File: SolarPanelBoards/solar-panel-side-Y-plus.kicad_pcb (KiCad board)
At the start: 2 copper layers, 82 x 99 mm, 24 parts, among them J1 Conn_01x06, U1 OPT3001DNPT

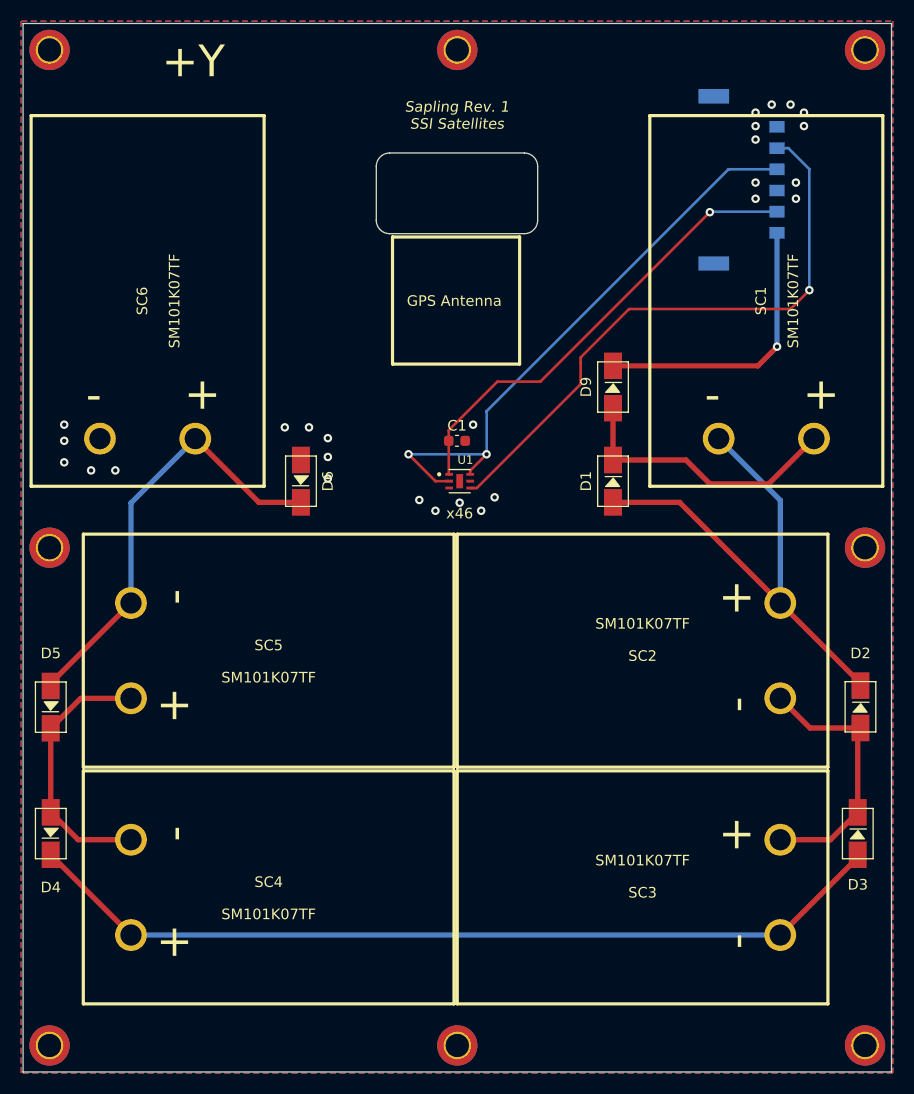
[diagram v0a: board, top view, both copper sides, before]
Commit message: Battery board and side panels ready for CAD check and review, pycubed not finished yet
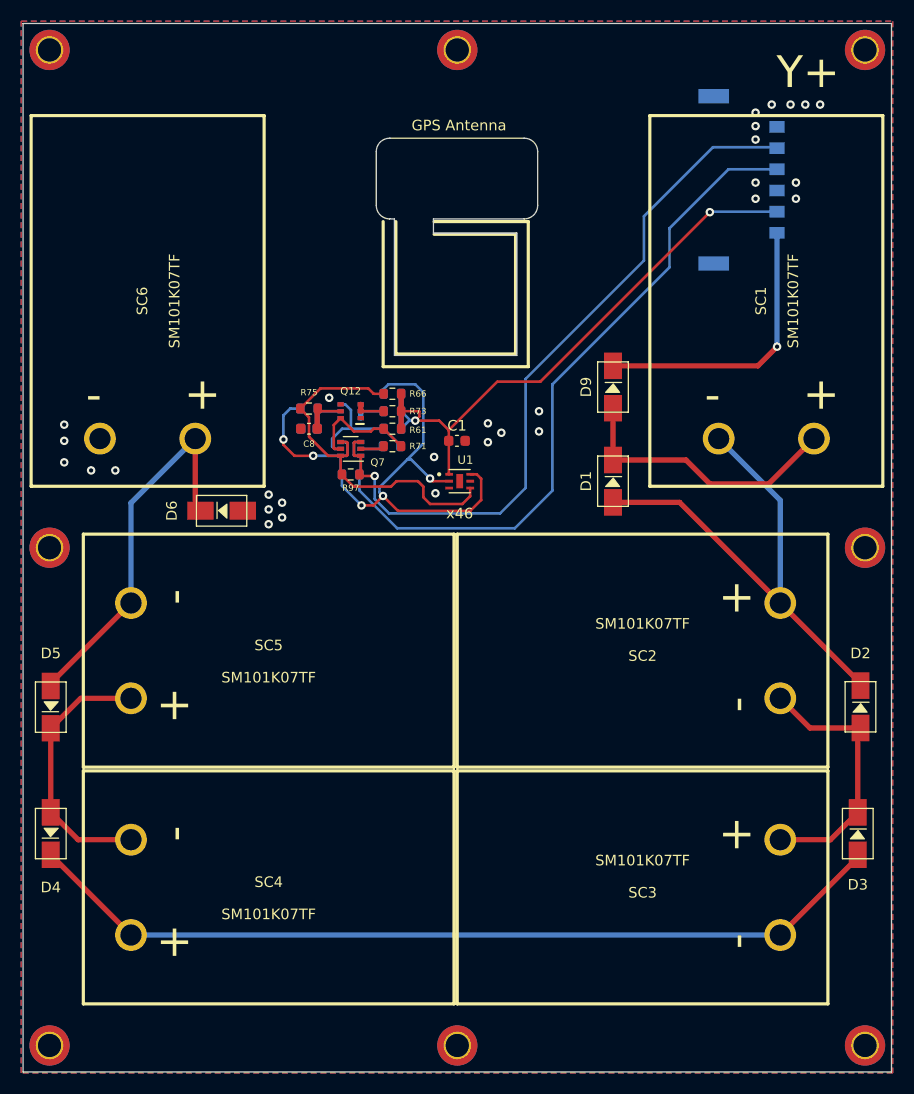
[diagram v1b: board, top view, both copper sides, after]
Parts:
- added C40: 10nF, Capacitor_SMD:C_0603_1608Metric, B.Cu at (134.6, 81.9)
- added C8: 10nF, Capacitor_SMD:C_0603_1608Metric, F.Cu at (134.6, 81.9)
- added Q12: BSS138DWQ-7, sapling:BSS138DWQ-7, F.Cu at (138.6, 80.3)
- added Q13: BSS138DWQ-7, sapling:BSS138DWQ-7, B.Cu at (138.6, 80.3)
- added Q7: MBT2222ADW1T1, Package_TO_SOT_SMD:SOT-363_SC-70-6, F.Cu at (138.6, 83.8)
- added Q8: MBT2222ADW1T1, Package_TO_SOT_SMD:SOT-363_SC-70-6, B.Cu at (138.6, 83.8)
- added R61: 10K, Resistor_SMD:R_0603_1608Metric, F.Cu at (142.5, 81.9)
- added R62: 10K, Resistor_SMD:R_0603_1608Metric, B.Cu at (142.5, 81.9)
- added R66: 10K, Resistor_SMD:R_0603_1608Metric, F.Cu at (142.5, 78.6)
- added R67: 10K, Resistor_SMD:R_0603_1608Metric, B.Cu at (142.5, 78.6)
- added R71: 680, Resistor_SMD:R_0603_1608Metric, F.Cu at (142.5, 83.6)
- added R72: 680, Resistor_SMD:R_0603_1608Metric, B.Cu at (142.4, 83.6)
- added R73: 100K, Resistor_SMD:R_0603_1608Metric, F.Cu at (142.5, 80.3)
- added R74: 100K, Resistor_SMD:R_0603_1608Metric, B.Cu at (142.5, 80.3)
- added R75: 200K, Resistor_SMD:R_0603_1608Metric, F.Cu at (134.6, 80.0)
- added R76: 200K, Resistor_SMD:R_0603_1608Metric, B.Cu at (134.6, 80.0)
- added R97: 0, Resistor_SMD:R_0603_1608Metric, F.Cu at (138.6, 86.2)
- added R98: 0, Resistor_SMD:R_0603_1608Metric, B.Cu at (138.6, 86.2)
- added REF**: AP.12F_Taoglas, sapling:AP.12F_Taoglas, F.Cu at (149.0, 61.1)
- moved D6 8.00 mm to (126.4, 89.7), turned to 0 degrees
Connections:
- U1 pad 2: SDA -> SDA_SUN
- U1 pad 4: SCL -> SCL_SUN
- U1 pad 6: SDA -> SDA_SUN
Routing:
- net SDA_SUN: track 0.00 -> 55.5 mm, vias 0 -> 5
- net SCL_SUN: track 0.00 -> 35.3 mm
- net +3V3: track 43.7 -> 60.0 mm, vias 1 -> 2
- net SDA: track 55.7 -> 68.8 mm, vias 2 -> 0
- net SCL: track 56.5 -> 69.4 mm
- net Net-(Q13-Pad6): track 0.00 -> 12.2 mm
- net Net-(Q12-Pad6): track 0.00 -> 10.8 mm
- net Net-(D5-Pad2): track 41.5 -> 36.0 mm
- net Net-(C8-Pad1): track 0.00 -> 4.19 mm
- net Net-(C40-Pad1): track 0.00 -> 4.19 mm
- net Net-(Q13-Pad2): track 0.00 -> 2.81 mm
- net Net-(Q12-Pad2): track 0.00 -> 2.81 mm
- net Net-(Q7-Pad2): track 0.00 -> 2.27 mm
- net Net-(Q8-Pad2): track 0.00 -> 2.20 mm
- net GND: vias 27 -> 29
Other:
- outline, holes or cut-outs redrawn
- board text added: "+3.3V"
- board text removed: "3.3"
- board text removed: "Sapling Rev. 1 SSI Satellites"

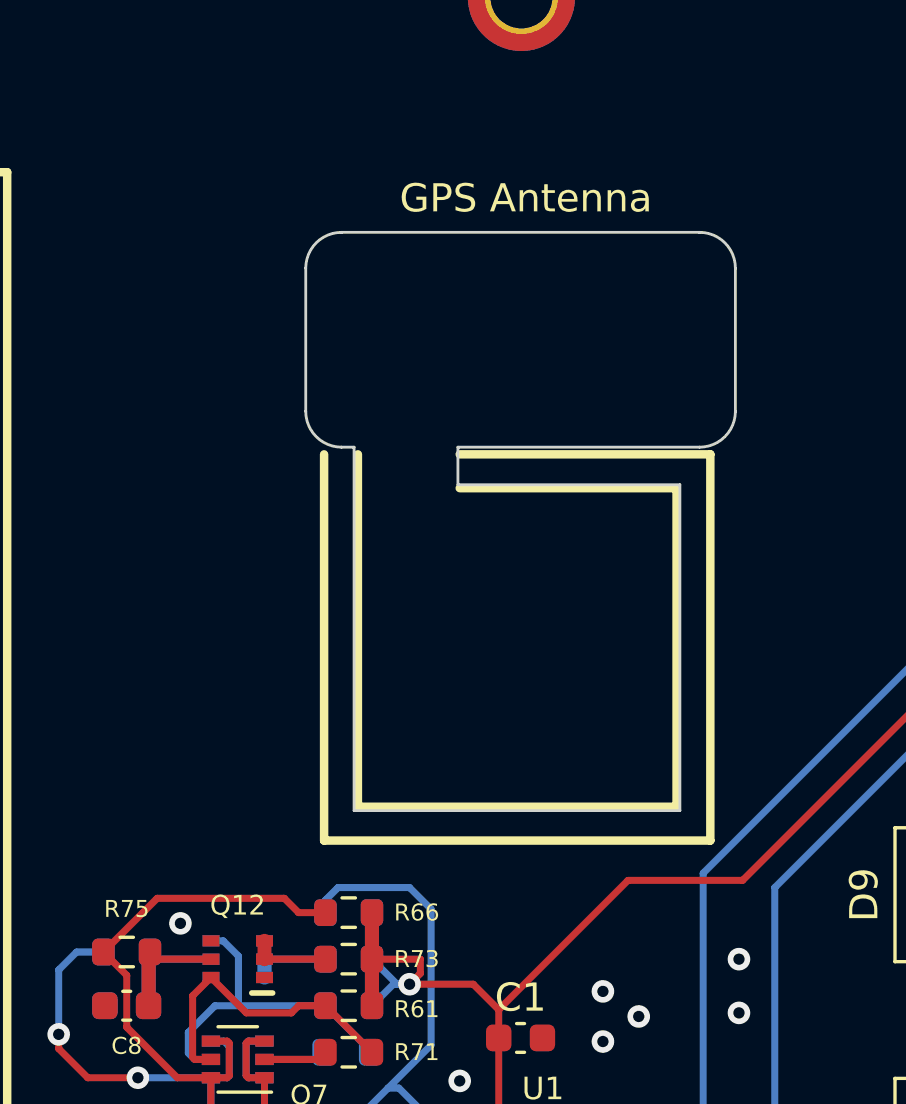
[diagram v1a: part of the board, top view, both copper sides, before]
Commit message: side panels ready except for RF trace width
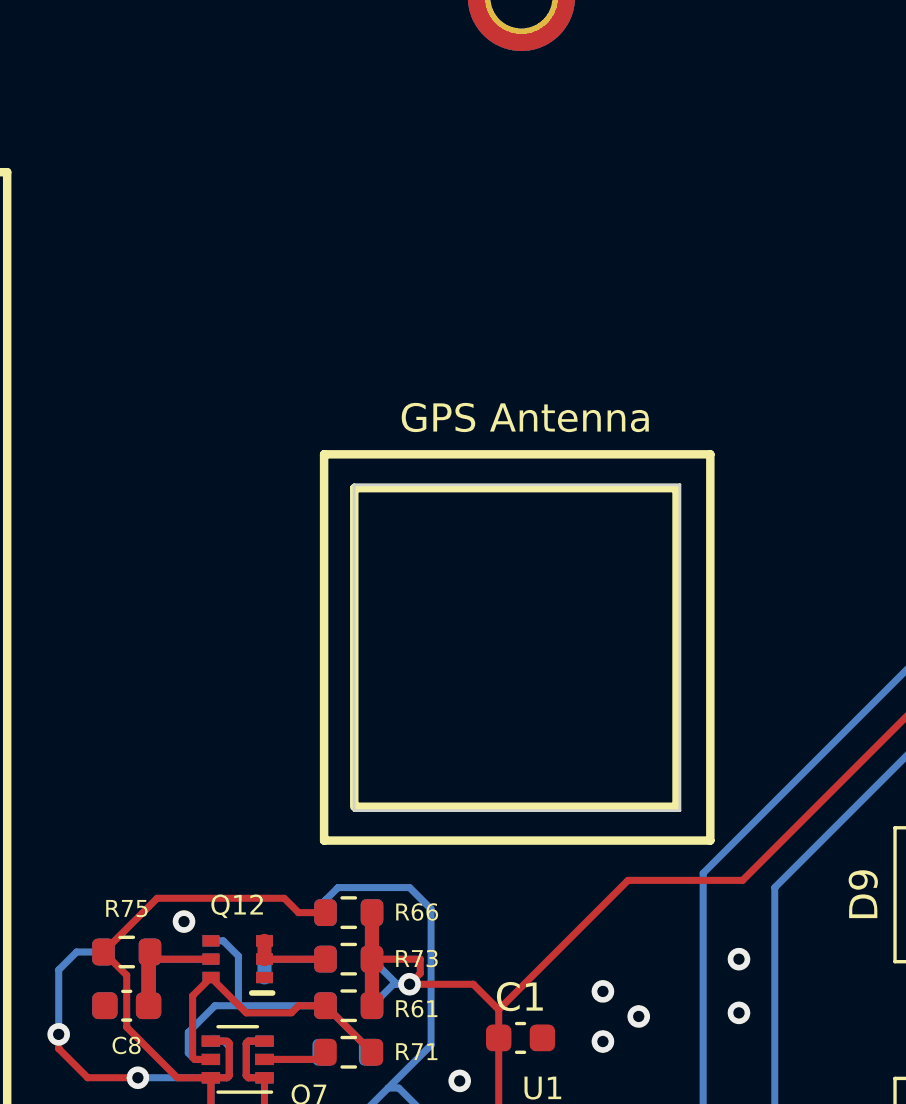
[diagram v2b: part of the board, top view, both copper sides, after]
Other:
- outline, holes or cut-outs redrawn
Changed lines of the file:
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@@
   (general
     (thickness 1.6)
-    (drawings 27)
+    (drawings 17)
     (tracks 244)
     (zones 0)
@@
       (effects (font (size 1 1) (thickness 0.15)))
     )
-    (fp_line (start -2.54 1.27) (end 6.35 1.27) (layer F.SilkS) (width 0.3))
+    (fp_line (start -6.28 13.77) (end -6.28 2.47) (layer F.SilkS) (width 0.3))
+    (fp_line (start -6.15 13.77) (end 5.15 13.77) (layer F.SilkS) (width 0.3))
+    (fp_line (start 5.15 13.77) (end 5.15 2.47) (layer F.SilkS) (width 0.3))
+    (fp_line (start -6.28 2.47) (end 5.15 2.47) (layer F.SilkS) (width 0.3))
+    (fp_line (start -7.35 14.97) (end -7.35 1.27) (layer F.SilkS) (width 0.3))
+    (fp_line (start -7.35 14.97) (end 6.35 14.97) (layer F.SilkS) (width 0.3))
     (fp_line (start 6.35 14.97) (end 6.35 1.27) (layer F.SilkS) (width 0.3))
-    (fp_line (start -7.35 14.97) (end 6.35 14.97) (layer F.SilkS) (width 0.3))
-    (fp_line (start -7.35 14.97) (end -7.35 1.27) (layer F.SilkS) (width 0.3))
-    (fp_line (start -2.54 2.47) (end 5.15 2.47) (layer F.SilkS) (width 0.3))
-    (fp_line (start -6.15 13.77) (end -6.15 1.27) (layer F.SilkS) (width 0.3))
-    (fp_line (start 5.15 13.77) (end 5.15 2.47) (layer F.SilkS) (width 0.3))
-    (fp_line (start -6.15 13.77) (end 5.15 13.77) (layer F.SilkS) (width 0.3))
+    (fp_line (start -7.35 1.27) (end 6.35 1.27) (layer F.SilkS) (width 0.3))
     (model C:/Users/grant/Downloads/AP.12F.07.0045A_Web_v2.step
-      (offset (xyz -4.75 20.3 70.7))
+      (offset (xyz -4.75 20.3 68.34999999999999))
       (scale (xyz 1 1 1))
       (rotate (xyz -180 0 -90))
@@
     )
   )
-  (gr_line (start 146.3675 62.103) (end 146.3675 63.4365) (layer Edge.Cuts) (width 0.1))
-  (gr_line (start 146.3675 62.103) (end 154.94 62.103) (layer Edge.Cuts) (width 0.1))
-  (gr_line (start 142.6845 74.9935) (end 142.6845 62.103) (layer Edge.Cuts) (width 0.1))
+  (gr_line (start 142.6845 74.9935) (end 142.6845 63.4365) (layer Edge.Cuts) (width 0.1))
   (gr_line (start 154.2415 74.9935) (end 142.6845 74.9935) (layer Edge.Cuts) (width 0.1))
   (gr_line (start 154.2415 63.4365) (end 154.2415 74.9935) (layer Edge.Cuts) (width 0.1))
-  (gr_line (start 146.3675 63.4365) (end 154.2415 63.4365) (layer Edge.Cuts) (width 0.1))
-  (gr_text "GPS Antenna" (at 148.7805 53.2765) (layer F.SilkS)
+  (gr_line (start 142.6845 63.4365) (end 154.2415 63.4365) (layer Edge.Cuts) (width 0.1))
+  (gr_text "GPS Antenna" (at 148.7805 61.087) (layer F.SilkS)
     (effects (font (size 1 1) (thickness 0.15)))
   )
@@
     (effects (font (size 0.7 0.7) (thickness 0.1)) (justify mirror))
   )
-  (gr_arc (start 142.24 60.833) (end 140.97 60.833) (angle -90) (layer Edge.Cuts) (width 0.1))
-  (gr_arc (start 142.24 55.753) (end 142.24 54.483) (angle -90) (layer Edge.Cuts) (width 0.1))
-  (gr_arc (start 154.94 55.753) (end 156.21 55.753) (angle -90) (layer Edge.Cuts) (width 0.1))
-  (gr_arc (start 154.94 60.833) (end 154.94 62.103) (angle -90) (layer Edge.Cuts) (width 0.1))
-  (gr_line (start 140.97 55.753) (end 140.97 60.833) (layer Edge.Cuts) (width 0.1))
-  (gr_line (start 154.94 54.483) (end 142.24 54.483) (layer Edge.Cuts) (width 0.1))
-  (gr_line (start 156.21 60.833) (end 156.21 55.753) (layer Edge.Cuts) (width 0.1))
-  (gr_line (start 142.24 62.103) (end 142.6845 62.103) (layer Edge.Cuts) (width 0.1))
   (gr_text x46 (at 148.844 89.916) (layer F.SilkS)
     (effects (font (size 1 1) (thickness 0.15)))
@@
   (via (at 151.511 83.185) (size 0.8) (drill 0.4) (layers F.Cu B.Cu) (net 1))
   (via (at 152.781 82.296) (size 0.8) (drill 0.4) (layers F.Cu B.Cu) (net 1))
-  (via (at 136.525 78.994) (size 0.8) (drill 0.4) (layers F.Cu B.Cu) (net 1))
+  (via (at 136.652 78.9305) (size 0.8) (drill 0.4) (layers F.Cu B.Cu) (net 1))
   (via (at 156.337 82.169) (size 0.8) (drill 0.4) (layers F.Cu B.Cu) (net 1))
   (via (at 156.337 80.264) (size 0.8) (drill 0.4) (layers F.Cu B.Cu) (net 1))
